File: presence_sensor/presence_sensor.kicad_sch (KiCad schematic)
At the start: 49 parts, among them J1 SG_UL, J10 SWITCH, J2 SG_UR, J3 SG_LL, J30 DIGITAL_OUT_5V, J31 OPTO_OUT, J4 SG_LR, J40 EXTERNAL_LOAD, J5 BRIDGE, J50 12V_IN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

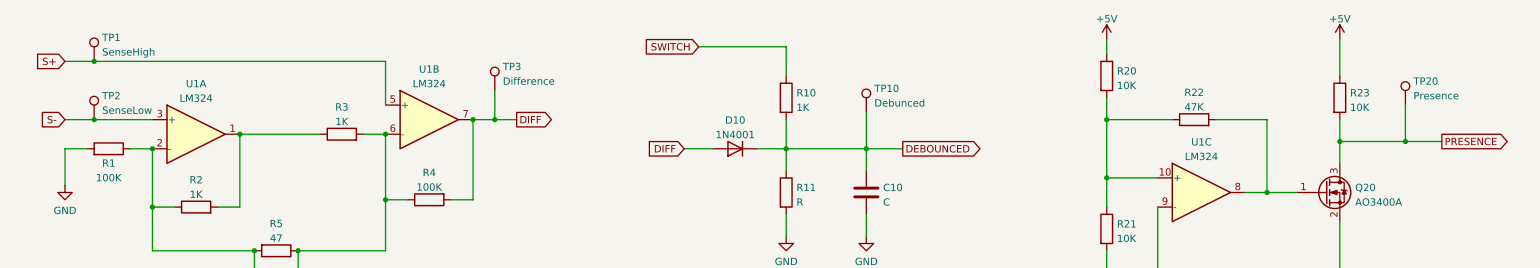
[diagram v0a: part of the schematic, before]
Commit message: Remove unneeded testpoints
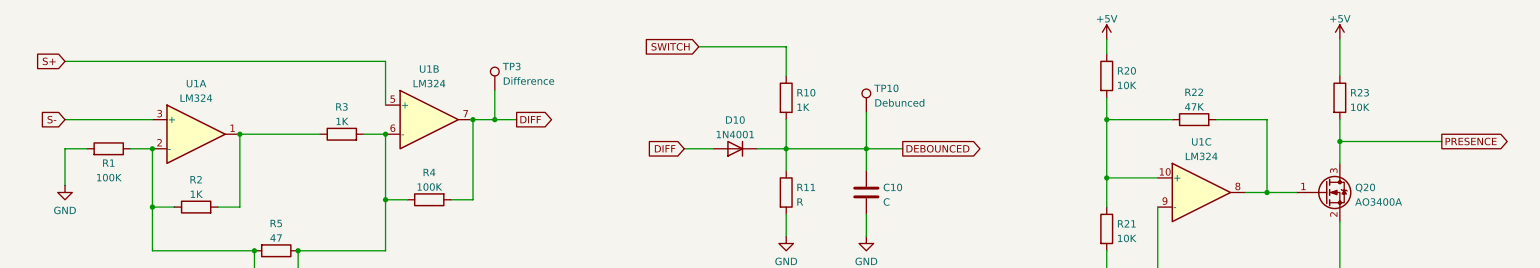
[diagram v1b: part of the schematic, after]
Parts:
- removed TP1: SenseHigh, TestPoint:TestPoint_Pad_D1.0mm, symbol Connector:TestPoint
- removed TP2: SenseLow, TestPoint:TestPoint_Pad_D1.0mm, symbol Connector:TestPoint
- removed TP20: Presence, TestPoint:TestPoint_Pad_D1.0mm, symbol Connector:TestPoint
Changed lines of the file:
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@@
   (junction (at 63.5 182.88) (diameter 0) (color 0 0 0 0)
   )
-  (junction (at 260.35 41.91) (diameter 0) (color 0 0 0 0)
-  )
   (junction (at 96.52 167.64) (diameter 0) (color 0 0 0 0)
   )
   (junction (at 120.65 182.88) (diameter 0) (color 0 0 0 0)
   )
-  (junction (at 31.75 38.1) (diameter 0) (color 0 0 0 0)
-  )
   (junction (at 82.55 40.64) (diameter 0) (color 0 0 0 0)
   )
@@
   (junction (at 234.95 129.54) (diameter 0) (color 0 0 0 0)
   )
-  (junction (at 31.75 27.94) (diameter 0) (color 0 0 0 0)
-  )
   (wire (pts (xy 120.65 182.88) (xy 133.35 182.88))
     (stroke (width 0) (type default) (color 0 0 0 0))
@@
     (stroke (width 0) (type default) (color 0 0 0 0))
   )
-  (wire (pts (xy 260.35 41.91) (xy 266.7 41.91))
+  (wire (pts (xy 248.92 41.91) (xy 266.7 41.91))
     (stroke (width 0) (type default) (color 0 0 0 0))
   )
@@
     (stroke (width 0) (type default) (color 0 0 0 0))
   )
-  (wire (pts (xy 31.75 27.94) (xy 82.55 27.94))
+  (wire (pts (xy 26.67 27.94) (xy 82.55 27.94))
     (stroke (width 0) (type default) (color 0 0 0 0))
   )
@@
     (stroke (width 0) (type default) (color 0 0 0 0))
   )
-  (wire (pts (xy 260.35 35.56) (xy 260.35 41.91))
-    (stroke (width 0) (type default) (color 0 0 0 0))
-  )
   (wire (pts (xy 41.91 119.38) (xy 41.91 125.73))
     (stroke (width 0) (type default) (color 0 0 0 0))
@@
     (stroke (width 0) (type default) (color 0 0 0 0))
   )
-  (wire (pts (xy 26.67 27.94) (xy 31.75 27.94))
-    (stroke (width 0) (type default) (color 0 0 0 0))
-  )
   (wire (pts (xy 82.55 138.43) (xy 82.55 129.54))
     (stroke (width 0) (type default) (color 0 0 0 0))
@@
     (stroke (width 0) (type default) (color 0 0 0 0))
   )
-  (wire (pts (xy 31.75 38.1) (xy 41.91 38.1))
-    (stroke (width 0) (type default) (color 0 0 0 0))
-  )
   (wire (pts (xy 57.15 168.91) (xy 69.85 168.91))
     (stroke (width 0) (type default) (color 0 0 0 0))
@@
     (stroke (width 0) (type default) (color 0 0 0 0))
   )
-  (wire (pts (xy 26.67 38.1) (xy 31.75 38.1))
+  (wire (pts (xy 26.67 38.1) (xy 41.91 38.1))
     (stroke (width 0) (type default) (color 0 0 0 0))
   )
@@
   )
   (wire (pts (xy 267.97 110.49) (xy 262.89 110.49))
-    (stroke (width 0) (type default) (color 0 0 0 0))
-  )
-  (wire (pts (xy 248.92 41.91) (xy 260.35 41.91))
     (stroke (width 0) (type default) (color 0 0 0 0))
   )
@@
     )
     (property "Datasheet" "" (id 3) (at 125.73 125.73 0)
-      (effects (font (size 1.27 1.27)) hide)
-    )
-    (pin "1")
-  )
-  (symbol (lib_id "Connector:TestPoint") (at 31.75 27.94 0) (unit 1)
-    (in_bom yes) (on_board yes) (fields_autoplaced)
-    (property "Reference" "TP1" (id 0) (at 33.147 23.8033 0)
-      (effects (font (size 1.27 1.27)) (justify left))
-    )
-    (property "Value" "SenseHigh" (id 1) (at 33.147 26.3402 0)
-      (effects (font (size 1.27 1.27)) (justify left))
-    )
-    (property "Footprint" "TestPoint:TestPoint_Pad_D1.0mm" (id 2) (at 36.83 27.94 0)
-      (effects (font (size 1.27 1.27)) hide)
-    )
-    (property "Datasheet" "~" (id 3) (at 36.83 27.94 0)
       (effects (font (size 1.27 1.27)) hide)
     )
@@
     (pin "2")
   )
-  (symbol (lib_id "Connector:TestPoint") (at 31.75 38.1 0) (unit 1)
-    (in_bom yes) (on_board yes) (fields_autoplaced)
-    (property "Reference" "TP2" (id 0) (at 33.147 33.9633 0)
-      (effects (font (size 1.27 1.27)) (justify left))
-    )
-    (property "Value" "SenseLow" (id 1) (at 33.147 36.5002 0)
-      (effects (font (size 1.27 1.27)) (justify left))
-    )
-    (property "Footprint" "TestPoint:TestPoint_Pad_D1.0mm" (id 2) (at 36.83 38.1 0)
-      (effects (font (size 1.27 1.27)) hide)
-    )
-    (property "Datasheet" "~" (id 3) (at 36.83 38.1 0)
-      (effects (font (size 1.27 1.27)) hide)
-    )
-    (pin "1")
-  )
   (symbol (lib_id "Device:R") (at 152.4 34.29 0) (unit 1)
     (in_bom yes) (on_board yes) (fields_autoplaced)
@@
     )
     (property "Datasheet" "" (id 3) (at 96.52 160.02 0)
-      (effects (font (size 1.27 1.27)) hide)
-    )
-    (pin "1")
-  )
-  (symbol (lib_id "Connector:TestPoint") (at 260.35 35.56 0) (unit 1)
-    (in_bom yes) (on_board yes) (fields_autoplaced)
-    (property "Reference" "TP20" (id 0) (at 261.747 31.4233 0)
-      (effects (font (size 1.27 1.27)) (justify left))
-    )
-    (property "Value" "Presence" (id 1) (at 261.747 33.9602 0)
-      (effects (font (size 1.27 1.27)) (justify left))
-    )
-    (property "Footprint" "TestPoint:TestPoint_Pad_D1.0mm" (id 2) (at 265.43 35.56 0)
-      (effects (font (size 1.27 1.27)) hide)
-    )
-    (property "Datasheet" "~" (id 3) (at 265.43 35.56 0)
       (effects (font (size 1.27 1.27)) hide)
     )
@@
       (reference "R100") (unit 1) (value "10K") (footprint "Resistor_SMD:R_1206_3216Metric_Pad1.30x1.75mm_HandSolder")
     )
-    (path "/51c4e930-6c6f-4e75-a658-84ce93b64dbe"
-      (reference "TP1") (unit 1) (value "SenseHigh") (footprint "TestPoint:TestPoint_Pad_D1.0mm")
-    )
-    (path "/96e1f2e5-0e78-4b7e-bdd3-46a1c6376e91"
-      (reference "TP2") (unit 1) (value "SenseLow") (footprint "TestPoint:TestPoint_Pad_D1.0mm")
-    )
     (path "/b05483dd-3114-4790-b2ac-ebeb336d89e3"
       (reference "TP3") (unit 1) (value "Difference") (footprint "TestPoint:TestPoint_Pad_D1.0mm")
@@
       (reference "TP10") (unit 1) (value "Debunced") (footprint "TestPoint:TestPoint_Pad_D1.0mm")
     )
-    (path "/9df55fd6-8644-4c09-8142-e1e6b2195cea"
-      (reference "TP20") (unit 1) (value "Presence") (footprint "TestPoint:TestPoint_Pad_D1.0mm")
-    )
     (path "/8338e846-812b-41c6-ad83-c397e10d62a8"
